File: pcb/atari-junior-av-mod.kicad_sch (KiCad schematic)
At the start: 32 parts

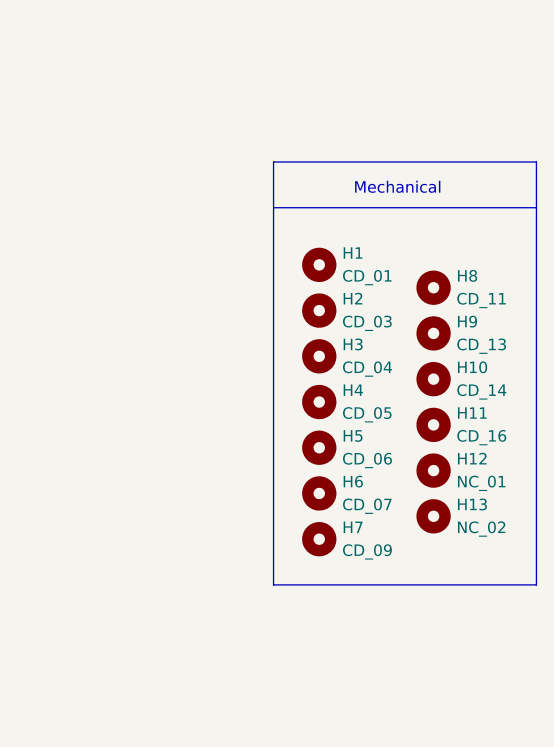
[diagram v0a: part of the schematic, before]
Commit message: Align mechanical components
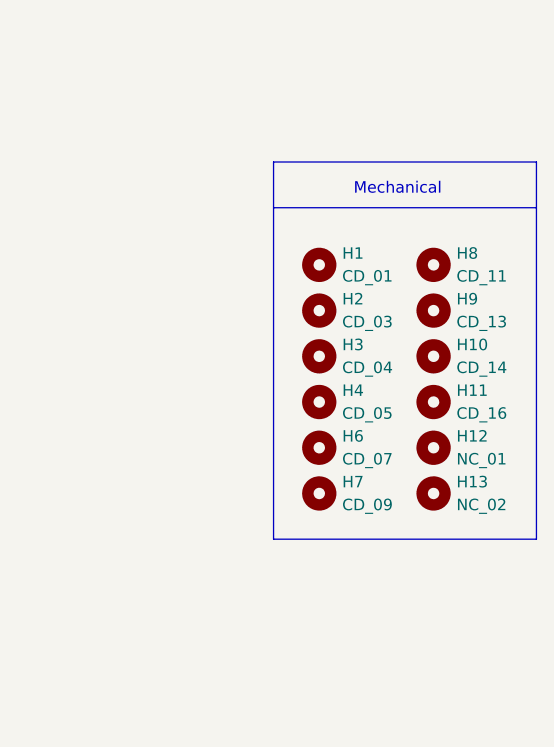
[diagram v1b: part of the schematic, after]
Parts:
- removed H5: CD_06, MeineBib:ModHole2mm, symbol Mechanical:MountingHole
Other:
- moved on the sheet: H10, H11, H12, H13, H6, H7, H8, H9

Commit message: Update BOM
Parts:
- C1: LCSC (none) -> C14858
- H1, H10, H11, H12, H13, H2, H3, H4, H6, H7, H8, H9, JP1, JP2, Pad1, Pad10, Pad11, Pad2, Pad3, Pad4, Pad5, Pad6, Pad7, Pad8, Pad9: now left out of the parts list
- R1: LCSC (none) -> C22978
- R2: LCSC (none) -> C4190
- R3: LCSC (none) -> C23138
- R4, R5: LCSC (none) -> C21190
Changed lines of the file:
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@@
   )
   (symbol (lib_id "Mechanical:MountingHole") (at 219.71 107.95 0) (unit 1)
-    (in_bom yes) (on_board yes) (fields_autoplaced)
+    (in_bom no) (on_board yes) (fields_autoplaced)
     (property "Reference" "H13" (id 0) (at 222.25 106.6799 0)
       (effects (font (size 1.27 1.27)) (justify left))
@@
   )
   (symbol (lib_id "Mechanical:MountingHole") (at 207.01 87.63 0) (unit 1)
-    (in_bom yes) (on_board yes) (fields_autoplaced)
+    (in_bom no) (on_board yes) (fields_autoplaced)
     (property "Reference" "H2" (id 0) (at 209.55 86.3599 0)
       (effects (font (size 1.27 1.27)) (justify left))
@@
   )
   (symbol (lib_id "Connector_Generic:Conn_01x01") (at 154.94 58.42 0) (unit 1)
-    (in_bom yes) (on_board yes) (fields_autoplaced)
+    (in_bom no) (on_board yes) (fields_autoplaced)
     (property "Reference" "Pad1" (id 0) (at 157.48 57.1499 0)
       (effects (font (size 1.27 1.27)) (justify left))
@@
   )
   (symbol (lib_id "Connector_Generic:Conn_01x01") (at 92.71 134.62 180) (unit 1)
-    (in_bom yes) (on_board yes)
+    (in_bom no) (on_board yes)
     (property "Reference" "Pad11" (id 0) (at 86.36 133.35 0))
     (property "Value" "CD_08" (id 1) (at 86.36 135.89 0))
@@
       (effects (font (size 1.27 1.27)) hide)
     )
+    (property "LCSC" "C22978" (id 4) (at 130.81 87.63 90)
+      (effects (font (size 1.27 1.27)) hide)
+    )
     (pin "1")
     (pin "2")
@@
       (effects (font (size 1.27 1.27)) hide)
     )
+    (property "LCSC" "C21190" (id 4) (at 139.7 128.27 90)
+      (effects (font (size 1.27 1.27)) hide)
+    )
     (pin "1")
     (pin "2")
   )
   (symbol (lib_id "Mechanical:MountingHole") (at 207.01 102.87 0) (unit 1)
-    (in_bom yes) (on_board yes)
+    (in_bom no) (on_board yes)
     (property "Reference" "H6" (id 0) (at 209.55 101.5999 0)
       (effects (font (size 1.27 1.27)) (justify left))
@@
       (effects (font (size 1.27 1.27)) hide)
     )
+    (property "LCSC" "C21190" (id 4) (at 130.81 102.87 90)
+      (effects (font (size 1.27 1.27)) hide)
+    )
     (pin "1")
     (pin "2")
   )
   (symbol (lib_id "Connector_Generic:Conn_01x01") (at 154.94 134.62 0) (unit 1)
-    (in_bom yes) (on_board yes) (fields_autoplaced)
+    (in_bom no) (on_board yes) (fields_autoplaced)
     (property "Reference" "Pad2" (id 0) (at 157.48 133.3499 0)
       (effects (font (size 1.27 1.27)) (justify left))
@@
   )
   (symbol (lib_id "Connector_Generic:Conn_01x01") (at 92.71 72.39 180) (unit 1)
-    (in_bom yes) (on_board yes)
+    (in_bom no) (on_board yes)
     (property "Reference" "Pad6" (id 0) (at 86.36 71.12 0))
     (property "Value" "CD_12" (id 1) (at 86.36 73.66 0))
@@
   )
   (symbol (lib_id "Connector_Generic:Conn_01x01") (at 92.71 121.92 180) (unit 1)
-    (in_bom yes) (on_board yes)
+    (in_bom no) (on_board yes)
     (property "Reference" "Pad10" (id 0) (at 86.36 120.65 0))
     (property "Value" "Color" (id 1) (at 86.36 123.19 0))
@@
   )
   (symbol (lib_id "Mechanical:MountingHole") (at 207.01 107.95 0) (unit 1)
-    (in_bom yes) (on_board yes) (fields_autoplaced)
+    (in_bom no) (on_board yes) (fields_autoplaced)
     (property "Reference" "H7" (id 0) (at 209.55 106.6799 0)
       (effects (font (size 1.27 1.27)) (justify left))
@@
   )
   (symbol (lib_id "Mechanical:MountingHole") (at 219.71 92.71 0) (unit 1)
-    (in_bom yes) (on_board yes) (fields_autoplaced)
+    (in_bom no) (on_board yes) (fields_autoplaced)
     (property "Reference" "H10" (id 0) (at 222.25 91.4399 0)
       (effects (font (size 1.27 1.27)) (justify left))
@@
   )
   (symbol (lib_id "Connector_Generic:Conn_01x01") (at 92.71 110.49 180) (unit 1)
-    (in_bom yes) (on_board yes)
+    (in_bom no) (on_board yes)
     (property "Reference" "Pad9" (id 0) (at 86.36 109.22 0))
     (property "Value" "CD_15" (id 1) (at 86.36 111.76 0))
@@
   )
   (symbol (lib_id "Mechanical:MountingHole") (at 207.01 92.71 0) (unit 1)
-    (in_bom yes) (on_board yes) (fields_autoplaced)
+    (in_bom no) (on_board yes) (fields_autoplaced)
     (property "Reference" "H3" (id 0) (at 209.55 91.4399 0)
       (effects (font (size 1.27 1.27)) (justify left))
@@
   )
   (symbol (lib_id "Connector_Generic:Conn_01x01") (at 92.71 80.01 180) (unit 1)
-    (in_bom yes) (on_board yes)
+    (in_bom no) (on_board yes)
     (property "Reference" "Pad7" (id 0) (at 86.36 78.74 0))
     (property "Value" "CD_06" (id 1) (at 86.36 81.28 0))
@@
   )
   (symbol (lib_id "Connector_Generic:Conn_01x01") (at 92.71 66.04 180) (unit 1)
-    (in_bom yes) (on_board yes)
+    (in_bom no) (on_board yes)
     (property "Reference" "Pad5" (id 0) (at 86.36 64.77 0))
     (property "Value" "CD_10" (id 1) (at 86.36 67.31 0))
@@
   )
   (symbol (lib_id "Mechanical:MountingHole") (at 219.71 102.87 0) (unit 1)
-    (in_bom yes) (on_board yes) (fields_autoplaced)
+    (in_bom no) (on_board yes) (fields_autoplaced)
     (property "Reference" "H12" (id 0) (at 222.25 101.5999 0)
       (effects (font (size 1.27 1.27)) (justify left))
@@
       (effects (font (size 1.27 1.27)) hide)
     )
+    (property "LCSC" "C14858" (id 4) (at 139.7 113.03 0)
+      (effects (font (size 1.27 1.27)) hide)
+    )
     (pin "1")
     (pin "2")
   )
   (symbol (lib_id "Mechanical:MountingHole") (at 219.71 97.79 0) (unit 1)
-    (in_bom yes) (on_board yes) (fields_autoplaced)
+    (in_bom no) (on_board yes) (fields_autoplaced)
     (property "Reference" "H11" (id 0) (at 222.25 96.5199 0)
       (effects (font (size 1.27 1.27)) (justify left))
@@
   )
   (symbol (lib_id "Mechanical:MountingHole") (at 207.01 97.79 0) (unit 1)
-    (in_bom yes) (on_board yes) (fields_autoplaced)
+    (in_bom no) (on_board yes) (fields_autoplaced)
     (property "Reference" "H4" (id 0) (at 209.55 96.5199 0)
       (effects (font (size 1.27 1.27)) (justify left))
@@
       (effects (font (size 1.27 1.27)) hide)
     )
+    (property "LCSC" "C4190" (id 4) (at 130.81 66.04 90)
+      (effects (font (size 1.27 1.27)) hide)
+    )
     (pin "1")
     (pin "2")
   )
   (symbol (lib_id "Mechanical:MountingHole") (at 219.71 82.55 0) (unit 1)
-    (in_bom yes) (on_board yes) (fields_autoplaced)
+    (in_bom no) (on_board yes) (fields_autoplaced)
     (property "Reference" "H8" (id 0) (at 222.25 81.2799 0)
       (effects (font (size 1.27 1.27)) (justify left))
@@
   )
   (symbol (lib_id "Connector_Generic:Conn_01x01") (at 154.94 66.04 0) (unit 1)
-    (in_bom yes) (on_board yes) (fields_autoplaced)
+    (in_bom no) (on_board yes) (fields_autoplaced)
     (property "Reference" "Pad3" (id 0) (at 157.48 64.7699 0)
       (effects (font (size 1.27 1.27)) (justify left))
@@
   )
   (symbol (lib_id "Mechanical:MountingHole") (at 219.71 87.63 0) (unit 1)
-    (in_bom yes) (on_board yes) (fields_autoplaced)
+    (in_bom no) (on_board yes) (fields_autoplaced)
     (property "Reference" "H9" (id 0) (at 222.25 86.3599 0)
       (effects (font (size 1.27 1.27)) (justify left))
@@
   )
   (symbol (lib_id "Mechanical:MountingHole") (at 207.01 82.55 0) (unit 1)
-    (in_bom yes) (on_board yes) (fields_autoplaced)
+    (in_bom no) (on_board yes) (fields_autoplaced)
     (property "Reference" "H1" (id 0) (at 209.55 81.2799 0)
       (effects (font (size 1.27 1.27)) (justify left))
@@
       (effects (font (size 1.27 1.27)) hide)
     )
+    (property "LCSC" "C23138" (id 4) (at 130.81 72.39 90)
+      (effects (font (size 1.27 1.27)) hide)
+    )
     (pin "1")
     (pin "2")
   )
   (symbol (lib_id "Connector_Generic:Conn_01x01") (at 92.71 58.42 180) (unit 1)
-    (in_bom yes) (on_board yes)
+    (in_bom no) (on_board yes)
     (property "Reference" "Pad4" (id 0) (at 86.36 57.15 0))
     (property "Value" "Audio" (id 1) (at 86.36 59.69 0))
@@
   )
   (symbol (lib_id "Jumper:SolderJumper_3_Open") (at 102.87 87.63 90) (unit 1)
-    (in_bom yes) (on_board yes)
+    (in_bom no) (on_board yes)
     (property "Reference" "JP1" (id 0) (at 100.33 86.3599 90)
       (effects (font (size 1.27 1.27)) (justify left))
@@
   )
   (symbol (lib_id "Jumper:SolderJumper_3_Open") (at 102.87 102.87 90) (unit 1)
-    (in_bom yes) (on_board yes)
+    (in_bom no) (on_board yes)
     (property "Reference" "JP2" (id 0) (at 100.33 101.5999 90)
       (effects (font (size 1.27 1.27)) (justify left))
@@
   )
   (symbol (lib_id "Connector_Generic:Conn_01x01") (at 92.71 95.25 180) (unit 1)
-    (in_bom yes) (on_board yes)
+    (in_bom no) (on_board yes)
     (property "Reference" "Pad8" (id 0) (at 86.36 93.98 0))
     (property "Value" "CD_02" (id 1) (at 86.36 96.52 0))
